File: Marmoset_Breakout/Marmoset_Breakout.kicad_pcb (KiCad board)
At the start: 2 copper layers, 71.1 x 78.7 mm, 43 parts, among them P1 CONN_01X05, P2 CONN_01X04, P3 CONN_01X04, Q1 DTC114YKA, Q2 DTC114YKA, U1 CONN_CHIP1, U2 CONN_DISPLAY, U3 PCF8563T/5, U4 CONN_AUDIO, U5 PAM8302A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

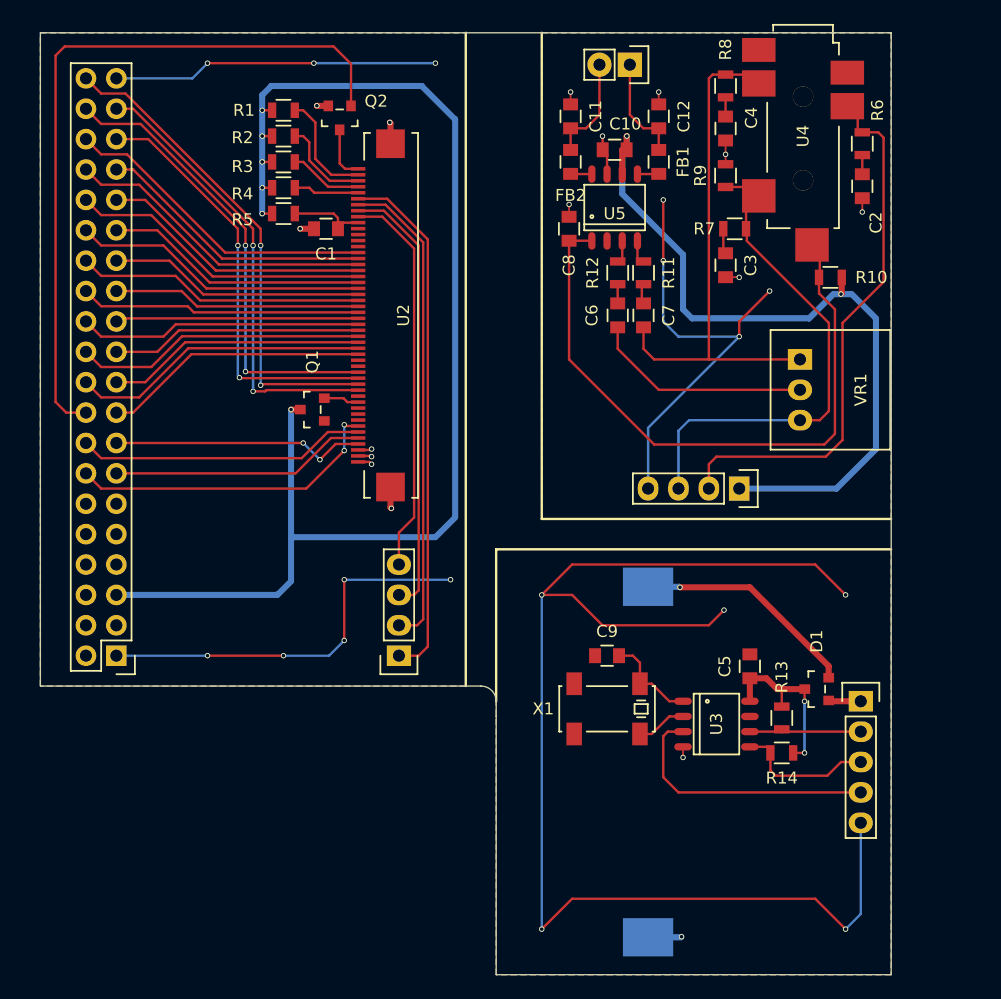
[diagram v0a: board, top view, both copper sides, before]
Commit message: Fixed unconnected LCD Power Enable signal. Fixed audio schematic and redid layout accordingly.
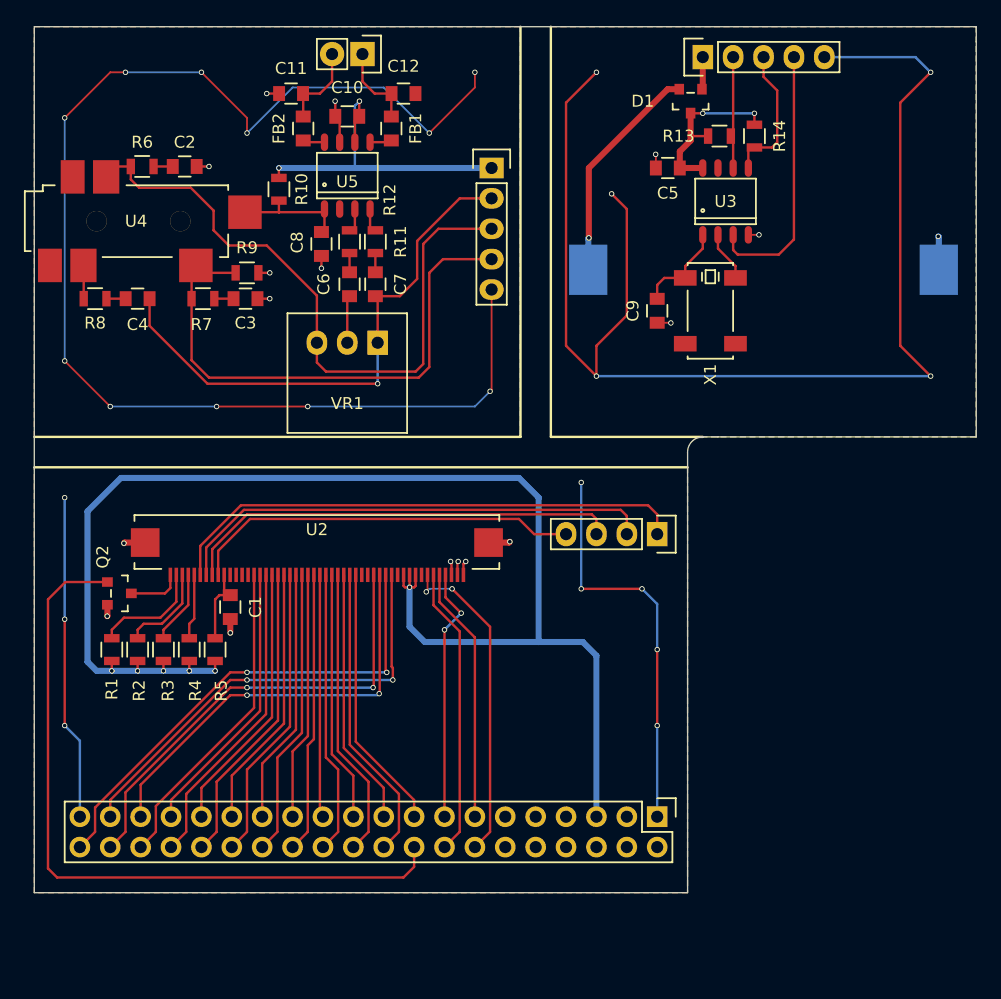
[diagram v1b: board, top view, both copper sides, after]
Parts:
- removed Q1: DTC114YKA, Marmoset:SOT-23-3
- P2: value CONN_01X04 -> CONN_01X05; footprint Pin_Headers:Pin_Header_Straight_1x04 -> Pin_Headers:Pin_Header_Straight_1x05
- moved R6 60.2 mm to (21.2, 23.9), turned to 0 degrees
- moved U4 60.0 mm to (17.4, 28.4), turned to 0 degrees
- moved C2 56.7 mm to (24.8, 23.9), turned to 0 degrees
- moved R8 55.6 mm to (17.3, 34.9), turned to 0 degrees
- moved P1 55.4 mm to (68.1, 14.7), turned to 90 degrees
- moved R14 51.6 mm to (72.4, 21.3), turned to 270 degrees
- moved C4 51.2 mm to (20.8, 34.9), turned to 0 degrees
- moved D1 50.3 mm to (67.1, 18.4), turned to 180 degrees
- moved R13 48.9 mm to (69.5, 21.3), turned to 0 degrees
- moved R1 47.3 mm to (18.7, 64.3), turned to 270 degrees
- moved U1 47.2 mm to (64.3, 78.2), turned to 270 degrees
- moved R10 46.7 mm to (32.6, 25.8), turned to 90 degrees
- moved R7 44.8 mm to (26.3, 34.9), turned to 0 degrees
- moved R2 44.6 mm to (20.8, 64.3), turned to 270 degrees
- moved Q2 43.8 mm to (19.3, 59.6), turned to 270 degrees
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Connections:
- C4 pad 2: /GND_A -> /HP_GND
- C7 pad 2: Net-(C7-Pad2) -> /HP_GND
- P2 pad 2: /HP_R -> /HP_GND
- P2 pad 3: /HP_L -> /HP_R
- P2 pad 4: /GND_A -> /HP_L
- R8 pad 1: Net-(C7-Pad2) -> Net-(R8-Pad1)
- U2 pad 40: Net-(Q1-Pad1) -> /+3V3_D
- U2 pad 41: Net-(Q1-Pad1) -> /+3V3_D
- U2 pad 42: Net-(Q1-Pad1) -> /+3V3_D
- U4 pad 4: Net-(C7-Pad2) -> Net-(R8-Pad1)
- VR1 pad 1: Net-(C7-Pad2) -> /HP_GND
- VR1 pad 3: /HP_L -> /HP_R
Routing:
- net /GND_A: track 49.0 -> 119.9 mm, vias 11 -> 17
- net /HP_GND: track 0.00 -> 45.7 mm, vias 0 -> 1
- net Net-(C8-Pad1): track 53.7 -> 9.93 mm
- net Net-(C7-Pad2): track 43.3 -> 0.00 mm
- net /+3V3_A: track 64.1 -> 27.8 mm
- net Net-(C6-Pad2): track 18.5 -> 3.97 mm
- net /HP_R: track 45.6 -> 55.4 mm
- net /+3V3_D: track 109.5 -> 116.7 mm
- net /HP_L: track 42.5 -> 46.1 mm
- net Net-(Q1-Pad1): track 2.97 -> 0.00 mm
- net Net-(R8-Pad1): track 0.00 -> 2.79 mm
- net /GND_C: track 112.9 -> 115.2 mm, vias 7 -> 9
- net Net-(C12-Pad2): track 8.88 -> 7.06 mm
- net Net-(C11-Pad2): track 8.88 -> 7.06 mm
- net Net-(C3-Pad1): track 2.13 -> 1.61 mm
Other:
- board size 71.1 x 78.7 mm -> 78.7 x 72.4 mm
- board text added: "HP_GND"
- board text added: "HP_L"
- board text added: "HP_R"
- board text removed: "L"
- board text removed: "R"

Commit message: Fixed Shutdown circuit for audio amp to use negative logic (as specified in datasheet) Fixed debouncing circuit for headphone ground pin. Added another pin to audio board to allow me to choose voltage for amplifier for testing. (I'm pretty sure it should be 3.3V but this will allow me to be sure) Updated layout accordingly.
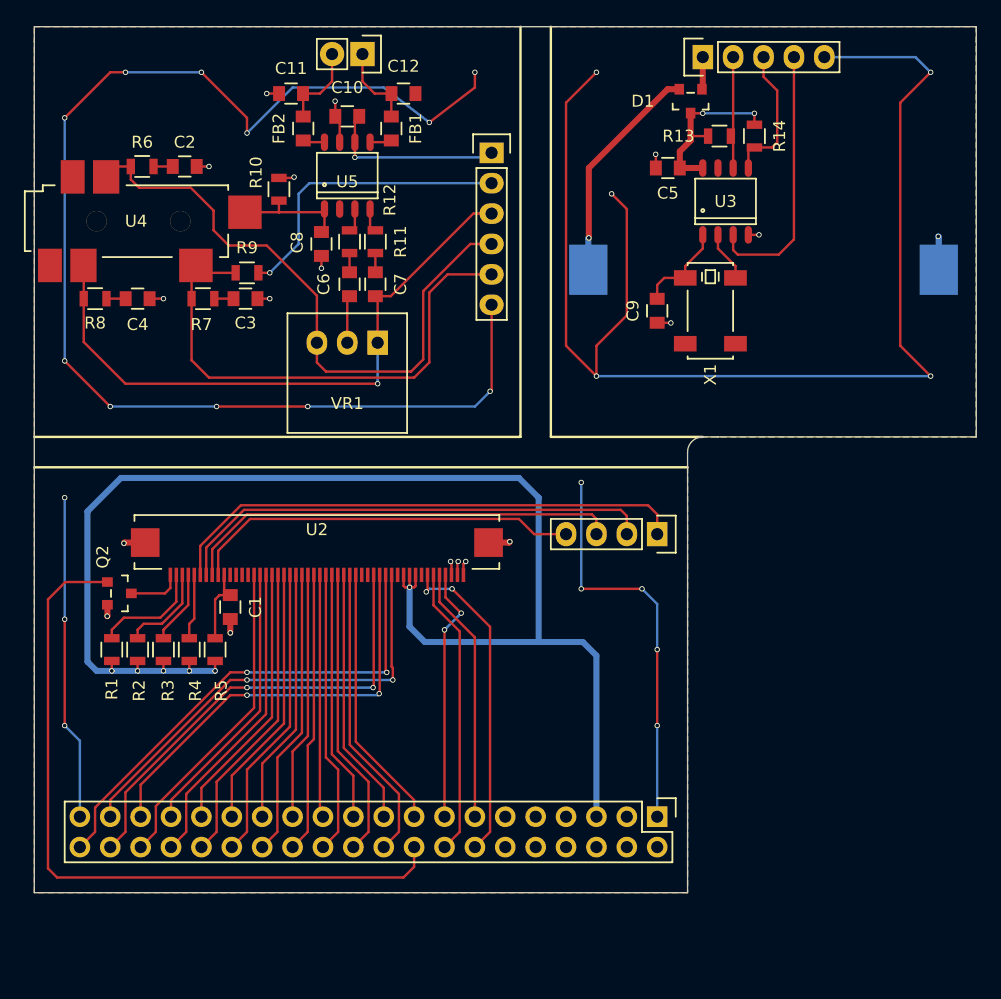
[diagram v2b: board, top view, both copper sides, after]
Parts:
- P2: value CONN_01X05 -> CONN_01X06; footprint Pin_Headers:Pin_Header_Straight_1x05 -> Pin_Headers:Pin_Header_Straight_1x06
- moved P2 1.27 mm to (50.4, 22.7)
- turned R10 to 270 degrees
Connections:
- C10 pad 2: /+3V3_A -> /V_AMP
- C4 pad 2: /HP_GND -> /GND_A
- P2 pad 1: /+3V3_A -> /V_AMP
- P2 pad 2: /HP_GND -> /+3V3_A
- P2 pad 3: /HP_R -> /HP_GND
- P2 pad 4: /HP_L -> /HP_R
- P2 pad 5: /GND_A -> /HP_L
- R10 pad 1: Net-(C8-Pad1) -> /GND_A
- R10 pad 2: /+3V3_A -> Net-(C8-Pad1)
- R8 pad 1: Net-(R8-Pad1) -> /HP_GND
- R9 pad 2: /GND_A -> /+3V3_A
- U4 pad 4: Net-(R8-Pad1) -> /HP_GND
- U5 pad 6: /+3V3_A -> /V_AMP
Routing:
- net /V_AMP: track 0.00 -> 15.2 mm, vias 0 -> 1
- net /HP_GND: track 45.7 -> 52.4 mm
- net /HP_R: track 55.4 -> 52.3 mm
- net Net-(R8-Pad1): track 2.79 -> 0.00 mm
- net /+3V3_A: track 27.8 -> 25.1 mm, vias 2 -> 1
- net /HP_L: track 46.1 -> 44.4 mm
- net /GND_A: track 119.9 -> 119.0 mm, vias 17 -> 18
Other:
- net class Default: trace_width 0.1524 -> 0.2032
- rule trace_min: 0.1524 -> 0.2032
- board text added: "2V5-5V0"

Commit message: Changed Speaker used and updated BOM/Schematic.
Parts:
- BT1: footprint Marmoset:BU2032-SM -> Marmoset:SMTU2032-LF
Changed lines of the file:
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@@
     (add_net "Net-(U5-Pad2)")
-  )
-  (module Marmoset:BU2032-SM (layer B.Cu)
-    (at 73.152 32.512)
-    (fp_text reference BT1 (at 0 -2.794) (layer B.SilkS)
-      (effects (font (size 1 1) (thickness 0.15)) (justify mirror))
-    )
-    (fp_text value BATT_2032 (at 0.127 0) (layer B.Fab)
-      (effects (font (size 1 1) (thickness 0.15)) (justify mirror))
-    )
-    (fp_text user - (at 7.239 0.254) (layer B.SilkS)
-      (effects (font (size 4 4) (thickness 0.15)) (justify mirror))
-    )
-    (fp_text user + (at -7.112 0.254) (layer B.SilkS)
-      (effects (font (size 4 4) (thickness 0.15)) (justify mirror))
-    )
-    (fp_circle (center 0 0) (end 11.2 0) (layer B.SilkS) (width 0.15))
-    (pad 2 smd rect (at 14.65 0) (size 3.2 4.2) (layers B.Cu B.Paste B.Mask)
-      (net 1 /GND_C))
-    (pad 1 smd rect (at -14.65 0) (size 3.2 4.2) (layers B.Cu B.Paste B.Mask)
-      (net 2 "Net-(BT1-Pad1)"))
   )
   (module Capacitors_SMD:C_0805 (layer F.Cu)
@@
     )
   )
+  (module Marmoset:SMTU2032-LF (layer B.Cu)
+    (at 73.152 32.512)
+    (fp_text reference BT1 (at 0 -2.794) (layer B.SilkS)
+      (effects (font (size 1 1) (thickness 0.15)) (justify mirror))
+    )
+    (fp_text value BATT_2032 (at 0.127 0) (layer B.Fab)
+      (effects (font (size 1 1) (thickness 0.15)) (justify mirror))
+    )
+    (fp_text user - (at 7.239 0.254) (layer B.SilkS)
+      (effects (font (size 4 4) (thickness 0.15)) (justify mirror))
+    )
+    (fp_text user + (at -7.112 0.254) (layer B.SilkS)
+      (effects (font (size 4 4) (thickness 0.15)) (justify mirror))
+    )
+    (fp_circle (center 0 0) (end 11.2 0) (layer B.SilkS) (width 0.15))
+    (pad 2 smd rect (at 14.7 0) (size 2.6 3.5) (layers B.Cu B.Paste B.Mask)
+      (net 1 /GND_C))
+    (pad 1 smd rect (at -14.7 0) (size 2.6 3.5) (layers B.Cu B.Paste B.Mask)
+      (net 2 "Net-(BT1-Pad1)"))
+  )
   (gr_text 2V5-5V0 (at 44.958 22.479 180) (layer B.SilkS)
     (effects (font (size 1 1) (thickness 0.15)) (justify mirror))
@@
     (effects (font (size 1 1) (thickness 0.15)) (justify mirror))
   )
+  (segment (start 87.802 32.512) (end 87.802 29.763) (width 0.508) (layer B.Cu) (net 1))
+  (via (at 87.757 29.718) (size 0.4524) (drill 0.3) (layers F.Cu B.Cu) (net 1))
+  (segment (start 87.802 29.763) (end 87.757 29.718) (width 0.508) (layer B.Cu) (net 1))
   (segment (start 64.151 24.003) (end 64.151 22.876) (width 0.2032) (layer F.Cu) (net 1))
   (via (at 64.135 22.86) (size 0.4524) (drill 0.3) (layers F.Cu B.Cu) (net 1))
@@
   (via (at 87.122 16.002) (size 0.4524) (drill 0.3) (layers F.Cu B.Cu) (net 1))
   (segment (start 85.852 14.732) (end 87.122 16.002) (width 0.2032) (layer B.Cu) (net 1))
-  (segment (start 87.802 32.512) (end 87.802 29.763) (width 0.508) (layer B.Cu) (net 1))
-  (via (at 87.757 29.718) (size 0.4524) (drill 0.3) (layers F.Cu B.Cu) (net 1))
-  (segment (start 87.802 29.763) (end 87.757 29.718) (width 0.508) (layer B.Cu) (net 1))
   (segment (start 71.882 29.591) (end 72.771 29.591) (width 0.2032) (layer F.Cu) (net 1))
   (via (at 72.771 29.591) (size 0.4524) (drill 0.3) (layers F.Cu B.Cu) (net 1))
@@
   (segment (start 16.322 34.925) (end 16.322 32.171) (width 0.2032) (layer F.Cu) (net 84))
   (segment (start 16.322 32.171) (end 16.299 32.148) (width 0.2032) (layer F.Cu) (net 84))
-  (segment (start 50.038 23.114) (end 38.989 23.114) (width 0.2032) (layer B.Cu) (net 85) (status 400000))
+  (segment (start 50.038 23.114) (end 38.989 23.114) (width 0.2032) (layer B.Cu) (net 85))
   (segment (start 38.989 23.114) (end 38.989 21.844) (width 0.2032) (layer F.Cu) (net 85))
   (via (at 38.989 23.114) (size 0.4524) (drill 0.3) (layers F.Cu B.Cu) (net 85))
-  (segment (start 50.038 23.114) (end 50.419 22.733) (width 0.2032) (layer B.Cu) (net 85) (status C00000))
+  (segment (start 50.038 23.114) (end 50.419 22.733) (width 0.2032) (layer B.Cu) (net 85))
   (segment (start 38.989 21.844) (end 38.989 20.05) (width 0.2032) (layer F.Cu) (net 85))
   (segment (start 38.989 20.05) (end 39.354 19.685) (width 0.2032) (layer F.Cu) (net 85))
